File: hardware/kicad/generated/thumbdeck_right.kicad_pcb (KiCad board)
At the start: 4 copper layers, 74.5 x 109.5 mm, 103 parts, among them J1 USB-C, J2 BRIDGE_16, J3 LiPo, SW1 SNAP7, SW10 SNAP7, SW11 SNAP7, SW12 SNAP7, SW13 SNAP7, SW14 SNAP7, SW15 SNAP7, SW16 SNAP7, SW17 SNAP7, SW18 SNAP7, SW19 SNAP7, SW2 SNAP7, SW20 SNAP7, SW21 SNAP7, SW22 SNAP7, SW23 SNAP7, SW24 SNAP7, SW25 SNAP7, SW26 SNAP7, SW27 SNAP7, SW28 SNAP7, SW29 SNAP7, SW3 SNAP7, SW30 SNAP7, SW31 SNAP7, SW32 SNAP7, SW33 SNAP7, SW34 SNAP7, SW35 SNAP7, SW36 SNAP7, SW37 SNAP7, SW4 SNAP7, SW5 SNAP7, SW6 SNAP7, SW7 SNAP7, SW8 SNAP7, SW9 SNAP7, U1 E73-2G4M08S1C, U2 MCP73831, U3 USBLC6-2SC6

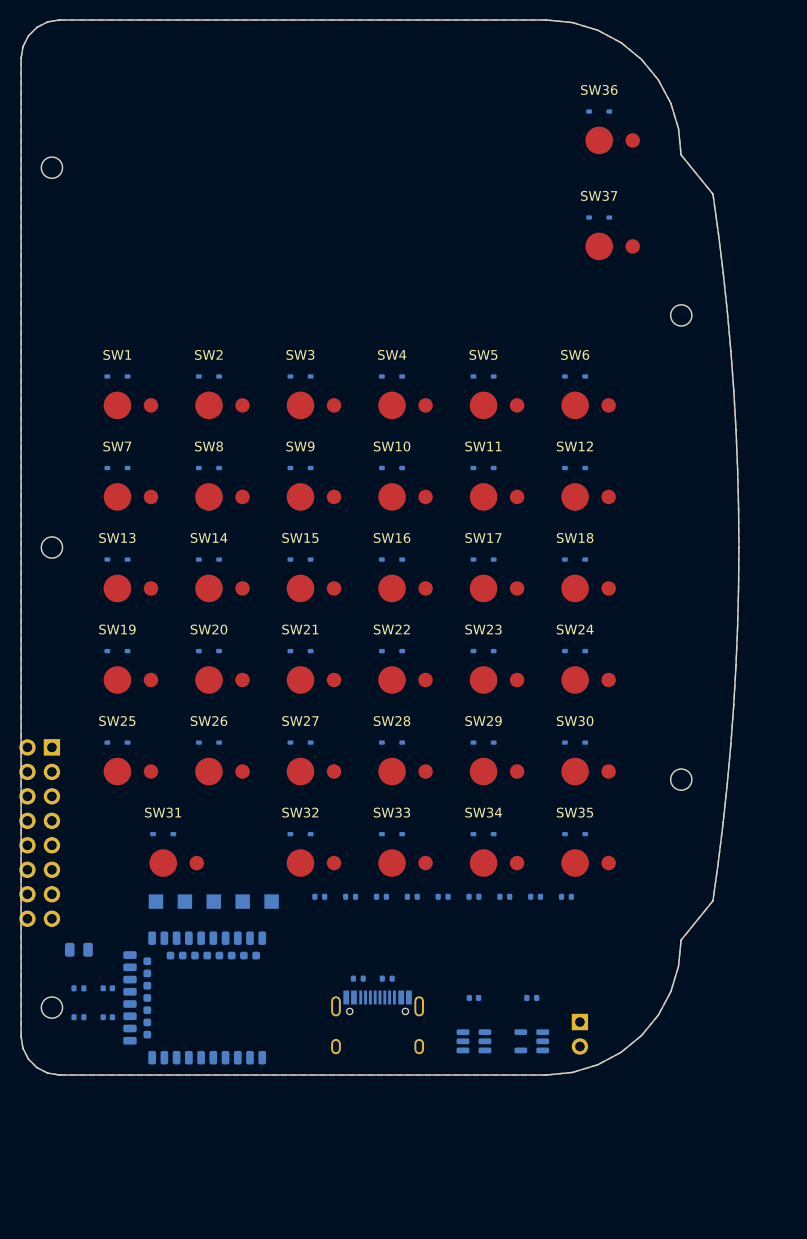
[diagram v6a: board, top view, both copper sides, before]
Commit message: rev-A (v0.15): production-ready boards, fab package, firmware, shells
Full top-to-bottom redesign pass driven by an 8-dimension adversarial audit
(120 findings, 14 blockers) and closed by a 6-agent verification review.

Boards (both DRC 0 violations / 0 unconnected, kicad-cli 9.0.9):
- Production snap-dome footprint: centre pad + 292° leg ring with 67.5° escape
  gap, mask apertures, pour + all-layer via keep-outs (old 2-pad proxy gave
  dead keys at 45° dome rotation)
- E73 rotated antenna-down at the bottom edge; keep-out verified copper-free
- Bridge: 16P 1.0mm FFC ZIF (AFA07-S16FCC-00) per grip + straight type-A
  jumper; left-grip nets assigned by ribbon geometry (proven 1:1)
- Battery: JST-PH SMT + MSK12C02 power switch (charger stays on cell side);
  reset tact (floor pinhole); charge LED on STAT; charger caps at the chip;
  SAADC filter cap; USB ESD inline; deterministic USB data-pair copper
  (interleaved pad pairs are un-autoroutable); COL9 off XL1 to P0.04;
  spare I2C broken out; boards grown to 76.5x114.5 (FFC + module-at-edge)
- Autonomous route loop rebuilt: Freerouting -Xss16m, In1 exported as power
  layer, obstacle-aware GND stitcher, generated GND escape vias, DRC-gated
  fab export (gerbers/BOM/CPL per board, JLC format, LCSC stamped)

Firmware (ZMK v0.3.0): 5 build-breakers fixed (west pin, pointing.h, DCDC
symbol, K32SRC_RC — BLE never started without it, nice!nano flash layout),
board moved to config/boards, FN layer gains -/=/Home/End/PrtSc + mouse keys
on the D-pad, self-contained CI workflow.

Mechanical: USB opening on the real connector, phone pocket + MagSafe ring
recess, PCB support posts, keymat clamp rim, switch slot + pinhole + LED
hole, cavity 6.3mm; fit-check 0 collisions with real part geometry.

Docs rewritten to rev-A reality; stale fab artifacts removed; renders
regenerated. Legacy route-finishing scripts retired to legacy/.

Co-Authored-By: Claude Fable 5 <noreply@anthropic.com>
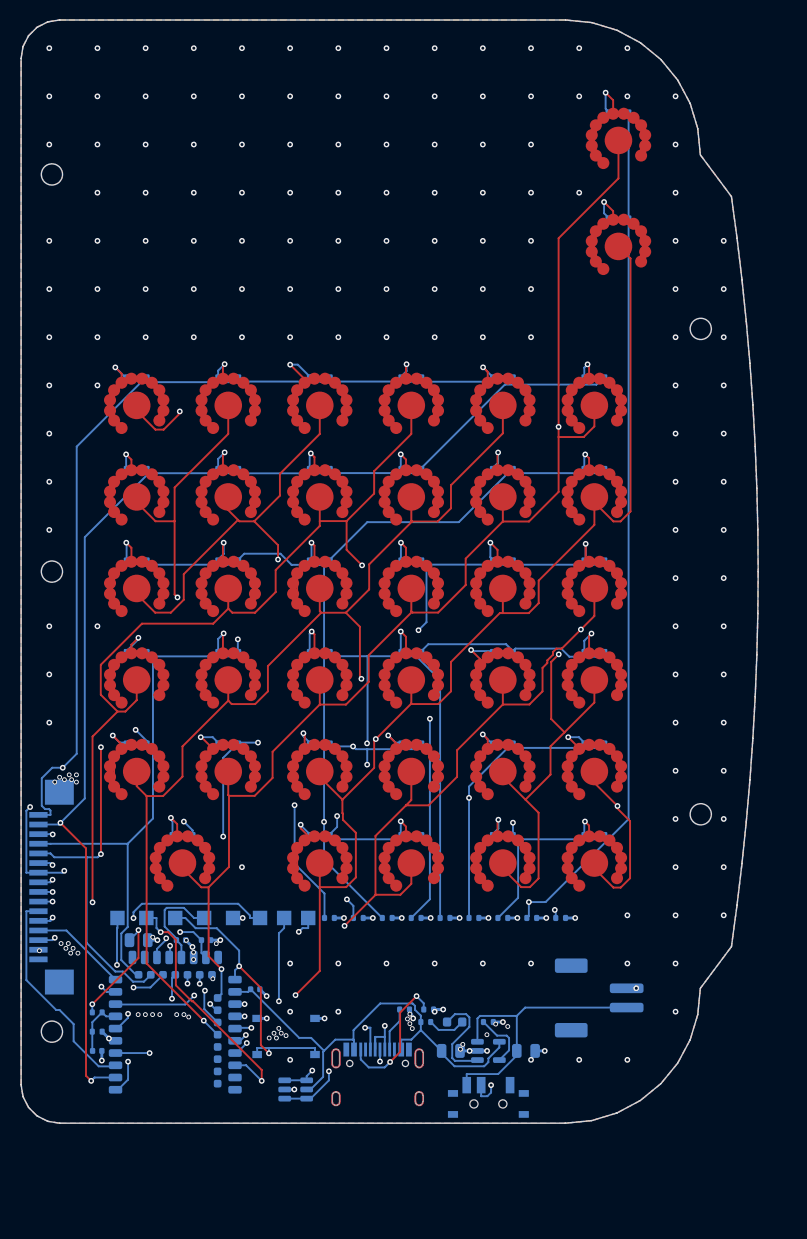
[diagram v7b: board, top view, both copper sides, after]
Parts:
- added C5: 4u7/0805, C_0805_2012Metric, B.Cu at (52.4, 107.0)
- added C6: 100nF, C_0402_1005Metric, B.Cu at (7.90, 107.0)
- added C7: 1uF, C_0402_1005Metric, B.Cu at (24.3, 100.6)
- added D80: LED_RED, LED_0603_1608Metric, B.Cu at (45.0, 104.0)
- added R25: 1k, R_0402_1005Metric, B.Cu at (42.0, 104.0)
- added SW90: MSK12C02, msk12c02_slide, B.Cu at (48.5, 112.5)
- added SW91: TS-1187A, SW_Push_1P1T_XKB_TS-1187A, B.Cu at (27.5, 105.5)
- added TP6: SDA, TestPoint_Pad_1.5x1.5mm, B.Cu at (24.8, 93.2)
- added TP7: SCL, TestPoint_Pad_1.5x1.5mm, B.Cu at (27.3, 93.2)
- added TP8: TP_INT, TestPoint_Pad_1.5x1.5mm, B.Cu at (29.8, 93.2)
- C3: value 4u7 -> 4u7/0805; footprint C_0402_1005Metric -> C_0805_2012Metric
- C4: value 4u7 -> 4u7/0805
- J2: value BRIDGE_16 -> FFC16; footprint PinHeader_2x08_P2.54mm_Vertical -> ffc_afa07_s16fcc
- J3: value LiPo -> JST-PH-2; footprint PinHeader_1x02_P2.54mm_Vertical -> JST_PH_S2B-PH-SM4-TB_1x02-1MP_P2.00mm_Horizontal
- SW1, SW10, SW11, SW12, SW13, SW14, SW15, SW16, SW17, SW18, SW19, SW2, SW20, SW21, SW22, SW23, SW24, SW25, SW26, SW27, SW28, SW29, SW3, SW30, SW31, SW32, SW33, SW34, SW35, SW36, SW37, SW4, SW5, SW6, SW7, SW8, SW9: footprint snaptron_7mm_simple -> snaptron_7mm_contact
- moved U3 19.2 mm to (28.5, 111.0), turned to 0 degrees
- moved J2 14.5 mm to (3.60, 90.0), turned to -90 degrees
- moved C2 11.4 mm to (19.2, 95.5), turned to 0 degrees
- moved C1 11.0 mm to (16.6, 95.5), turned to 0 degrees
- moved C4 6.28 mm to (12.2, 95.5), turned to 0 degrees
- moved U1 6.02 mm to (16.0, 106.0), turned to 0 degrees
- moved C3 6.00 mm to (44.6, 107.0), turned to 0 degrees
- moved R20 5.77 mm to (39.8, 102.7), turned to 0 degrees
- moved J1 5.40 mm to (37.0, 110.9)
- moved R21 5.36 mm to (42.3, 102.7), turned to 0 degrees
- moved R24 5.15 mm to (48.5, 104.0), turned to 0 degrees
- moved R23 4.88 mm to (7.90, 105.0), turned to 0 degrees
- moved U2 4.61 mm to (48.5, 107.0), turned to 0 degrees
- moved TP1 4.35 mm to (10.0, 93.2), turned to 0 degrees
- moved TP2 4.35 mm to (13.0, 93.2), turned to 0 degrees
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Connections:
- J3 pad 1: VBAT -> VBAT_CELL
- U1 pad 11: COL9 -> (no net)
- U1 pad 15: (no net) -> SDA
- U1 pad 18: (no net) -> COL9
- U1 pad 4: (no net) -> SCL
- U1 pad 8: (no net) -> TP_INT
- U2 pad 1: (no net) -> STAT
- U2 pad 3: VBAT -> VBAT_CELL
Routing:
- net COL1: track 0.00 -> 181.8 mm, vias 0 -> 4
- net COL0: track 0.00 -> 181.1 mm, vias 0 -> 3
- net COL3: track 0.00 -> 180.2 mm, vias 0 -> 4
- net ROW0: track 0.00 -> 171.4 mm, vias 0 -> 3
- net ROW1: track 0.00 -> 161.4 mm, vias 0 -> 3
- net COL2: track 0.00 -> 159.3 mm, vias 0 -> 4
- net COL4: track 0.00 -> 158.0 mm, vias 0 -> 3
- net ROW2: track 0.00 -> 151.9 mm, vias 0 -> 3
- net ROW7: track 0.00 -> 150.6 mm, vias 0 -> 3
- net ROW4: track 0.00 -> 134.4 mm, vias 0 -> 4
- net ROW3: track 0.00 -> 132.5 mm, vias 0 -> 3
- net ROW5: track 0.00 -> 125.5 mm, vias 0 -> 7
- net ROW6: track 0.00 -> 117.1 mm, vias 0 -> 6
- net VBAT: track 0.00 -> 69.2 mm, vias 0 -> 4
- net ROW8: track 0.00 -> 63.7 mm, vias 0 -> 3
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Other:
- board size 74.5 x 109.5 mm -> 76.5 x 114.5 mm
- board text added: "+"
- board text added: "-"
- board text added: "3V3"
- board text added: "BAT"
- board text added: "CHG"
- board text added: "GND"
- board text added: "INT"
- board text added: "J2 FFC16 <- pin1"
- board text added: "PWR"
- board text added: "RESET"
- board text added: "RST"
- board text added: "SCL"
- board text added: "SDA"
- board text added: "SWDCLK"
- board text added: "SWDIO"

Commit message: v0.17: Rii-proportioned grips — chin cut, electronics to top, rectangular keys
Print-in-hand feedback on the right grip lid: the device towered over both the
phone (~80mm) and the Rii i8+ (~97mm) the layout mimics, with the excess in the
chin below the space row. This rev takes the grip 114.5 -> 97.0mm to match the
i8+, verified end-to-end.

PCB / 2D (both boards re-routed, 0 DRC violations / 0 unconnected):
- bottom_strip 19 -> 7: chin under the space row ~23 -> ~9mm
- rectangular keycaps 8.5 x 7.0 (2u space 18.5) at 10 x 9mm pitch (was 8x8 @ 9.5)
- E73 + entire power front-end relocated to the top zone (vacated trackpad space)
  as a rigid 180-deg rotation of the DRC-verified rev-A cluster (hand-routed USB
  copper carried along); antenna now UP off the centre-top edge; USB-C mouth +
  power-switch knob in the top wall; JST-PH in the chin; PgUp/PgDn inner-top
- top-outer corner sharpened r14 -> r10 (squarer i8+-like shoulders)
- fab package, firmware (byte-identical - matrix/pinmap unchanged) regenerated
- new verify_alignment.py: machine audit PCB<->model<->caps<->shell (all pass);
  switch re-evaluated and KEPT (Snaptron 7mm; sample light-force ~160-180gf)

3D (deck3d.py regenerated + fit-checked: 203 bodies, 0 collisions, all bed-fit):
- keymat plungers / lid openings now the real rounded-rect caps (cluster round)
- USB-C opening, switch slot, antenna wall relief moved to the top wall; knob
  direction derived from placed rotation; panel screws derived from pocket span
  (old y=105 floated off the 97mm shell)
- fixed latent v0.16 bug: cluster plungers were disconnected islands - web now
  grows the 3mm living-hinge strips the 2D concept drew + asserts connectivity
- fixed deck.product() origin rounding (0.003mm seam offset tripped frame assert)

Renders regenerated (2D + 3D); 15 obsolete orphan renders removed; docs + README
updated throughout.

Co-Authored-By: Claude Opus 4.8 (1M context) <noreply@anthropic.com>
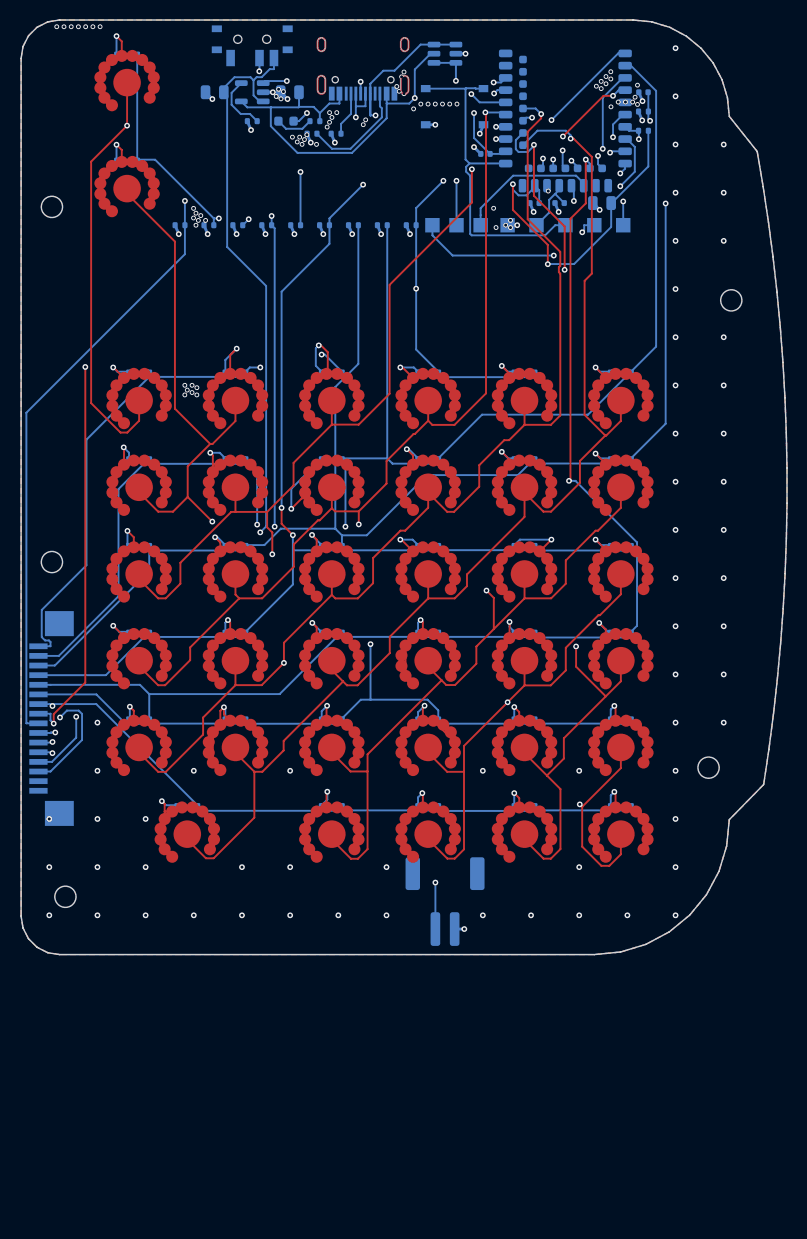
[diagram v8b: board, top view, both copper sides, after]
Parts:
- moved C6 114.5 mm to (64.6, 7.50), turned to 180 degrees
- moved SW90 113.2 mm to (24.0, 2.00), turned to 180 degrees
- moved R23 111.1 mm to (64.6, 9.50), turned to 180 degrees
- moved U3 108.6 mm to (44.0, 3.50), turned to 180 degrees
- moved R22 107.6 mm to (64.6, 11.5), turned to 180 degrees
- moved J1 107.3 mm to (35.5, 3.60), turned to 0 degrees
- moved U1 105.6 mm to (56.5, 8.50), turned to 180 degrees
- moved C5 104.6 mm to (20.1, 7.50), turned to 180 degrees
- moved U2 102.5 mm to (24.0, 7.50), turned to 180 degrees
- moved C3 100.9 mm to (27.9, 7.50), turned to 180 degrees
- moved SW91 98.1 mm to (45.0, 9.00), turned to 180 degrees
- moved R24 96.7 mm to (24.0, 10.5), turned to 180 degrees
- moved D80 95.1 mm to (27.5, 10.5), turned to 180 degrees
- moved R25 94.2 mm to (30.5, 10.5), turned to 180 degrees
- moved R21 91.7 mm to (30.2, 11.8), turned to 180 degrees
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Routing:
- net COL9: track 19.2 -> 102.5 mm
- net COL8: track 10.1 -> 92.7 mm, vias 0 -> 2
- net COL7: track 13.4 -> 94.0 mm
- net COL5: track 28.6 -> 107.9 mm
- net COL6: track 22.5 -> 100.1 mm, vias 0 -> 2
- net VBAT_CELL: track 29.6 -> 107.2 mm, vias 0 -> 2
- net ROW6: track 117.1 -> 164.1 mm, vias 6 -> 3
- net ROW0: track 171.4 -> 126.4 mm, vias 3 -> 5
- net COL0: track 181.1 -> 221.8 mm, vias 3 -> 2
- net ROW8: track 63.7 -> 102.7 mm, vias 3 -> 2
- net ROW5: track 125.5 -> 155.4 mm, vias 7 -> 4
- net ROW7: track 150.6 -> 122.9 mm, vias 3 -> 4
- net ROW4: track 134.4 -> 161.1 mm, vias 4 -> 3
- net COL1: track 181.8 -> 207.4 mm
- net COL3: track 180.2 -> 160.7 mm, vias 4 -> 3
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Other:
- board size 76.5 x 114.5 mm -> 79.5 x 97 mm
